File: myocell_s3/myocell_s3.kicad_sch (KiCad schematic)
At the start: 14 parts, among them J1 Conn_01x08, J5 Battery Connector JC2, J7 USB_C_Receptacle_USB2.0_16P

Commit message: scheme main table updated
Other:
- title: MYOCELL 8: EMG ADC board -> MYOCELL_S3: EMG ADC board
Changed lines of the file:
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@@
 	(paper "A4")
 	(title_block
-		(title "MYOCELL 8: EMG ADC board")
-		(date "2024-10-17")
+		(title "MYOCELL_S3: EMG ADC board")
+		(date "2025-12-24")
 		(rev "Rev 01")
 		(company "MIREA")
-		(comment 1 "2-8 ADC channels based on ADS1292(8)")
-		(comment 2 "CPU: ESP32 WROOM")
+		(comment 1 "4(8) ADC channels based on ADS1298")
+		(comment 2 "CPU: ESP32-S3 WROOM")
 	)
 	(text "esp32-s3 is spi master\nmiso - master in, slave out\nmosi - master out, slave in"

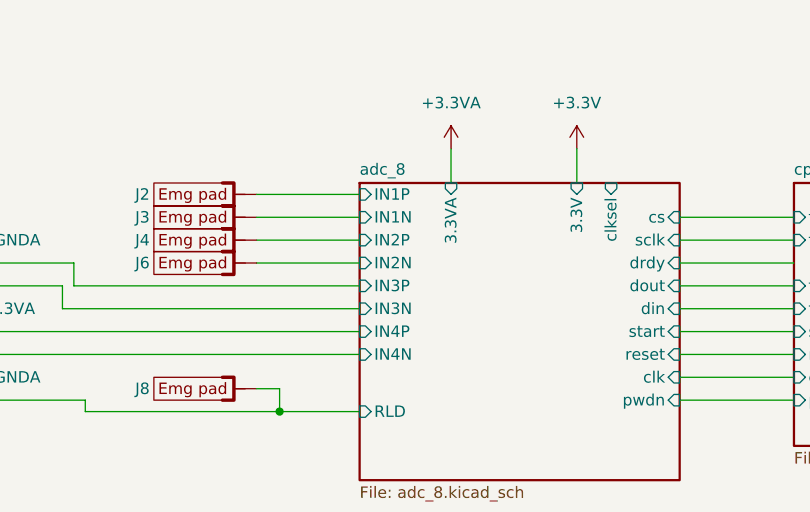
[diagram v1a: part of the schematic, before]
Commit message: emg filters updated
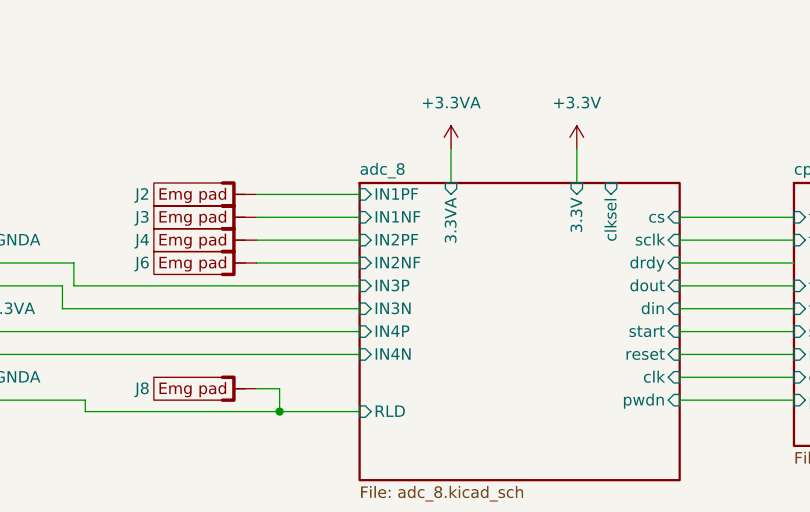
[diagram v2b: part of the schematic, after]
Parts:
- J2, J3, J4, J6, J8: value (none) -> ~
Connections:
- net adc_8/IN1N renamed adc_8/IN1NF
- net adc_8/IN1P renamed adc_8/IN1PF
- net adc_8/IN2N renamed adc_8/IN2NF
- net adc_8/IN2P renamed adc_8/IN2PF
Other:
- sheet adc_8 ports: added IN1NF, IN1PF, IN2NF, IN2PF; removed IN1N, IN1P, IN2N, IN2P

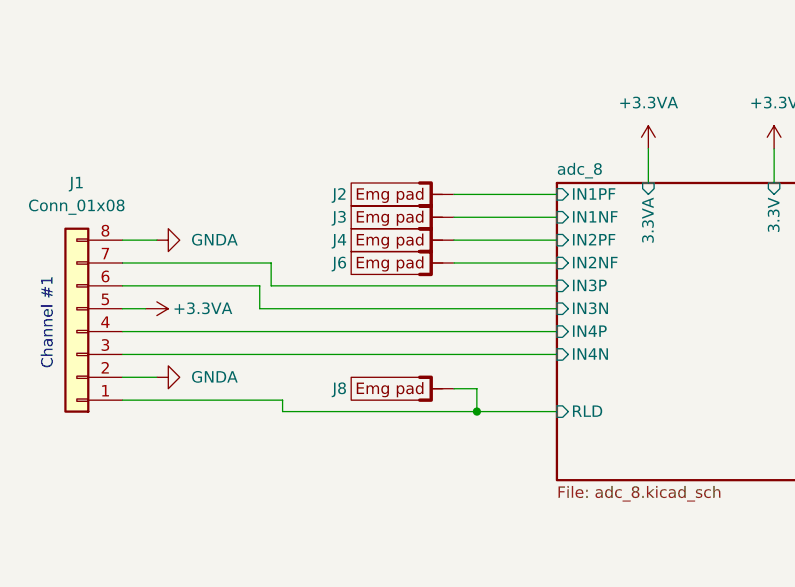
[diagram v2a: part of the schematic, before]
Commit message: schematic updated: channels 3,4 is onboard now
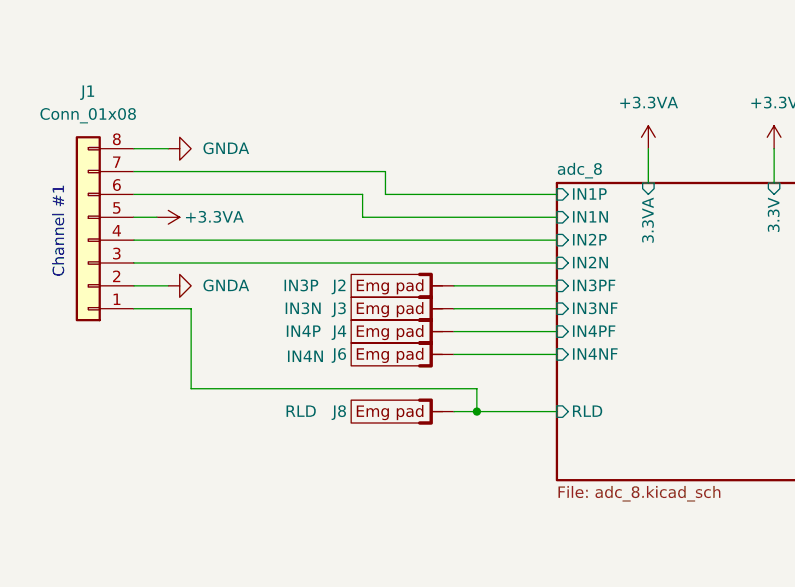
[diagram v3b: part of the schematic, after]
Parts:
- J2: value ~ -> IN3P
- J3: value ~ -> IN3N
- J4: value ~ -> IN4P
- J6: value ~ -> IN4N
- J8: value ~ -> RLD
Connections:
- net adc_8/IN1NF renamed adc_8/IN3NF
- net adc_8/IN1PF renamed adc_8/IN3PF
- net adc_8/IN2NF renamed adc_8/IN4NF
- net adc_8/IN2PF renamed adc_8/IN4PF
- net adc_8/IN3N renamed adc_8/IN1N
- net adc_8/IN3P renamed adc_8/IN1P
- net adc_8/IN4N renamed adc_8/IN2N
- net adc_8/IN4P renamed adc_8/IN2P
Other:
- sheet adc_8 ports: added IN1N, IN1P, IN2N, IN2P, IN3NF, IN3PF, IN4NF, IN4PF; removed IN1NF, IN1PF, IN2NF, IN2PF, IN3N, IN3P, IN4N, IN4P
- moved on the sheet: J1, J2, J3, J4, J6, J8

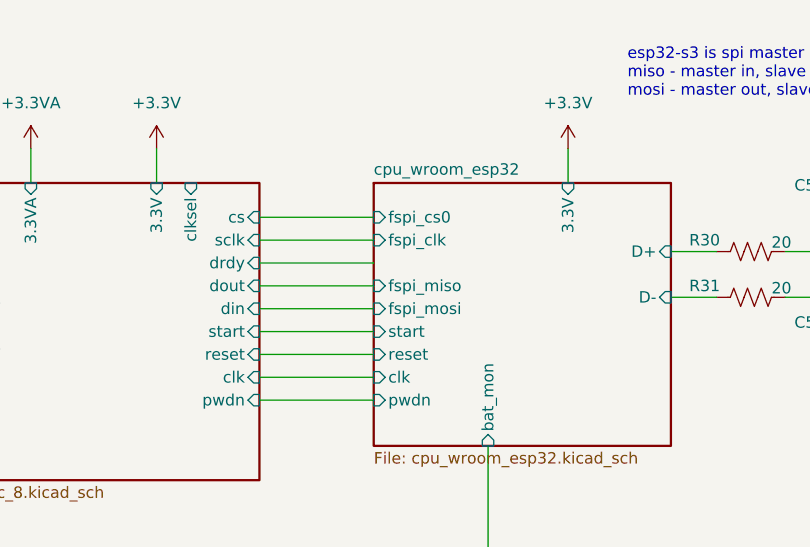
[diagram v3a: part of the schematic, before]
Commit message: drdy fixed
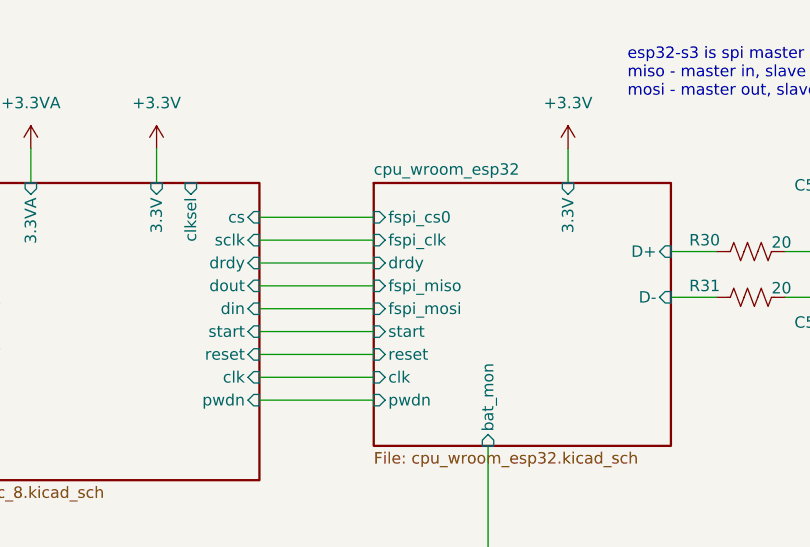
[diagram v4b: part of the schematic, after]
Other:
- sheet cpu_wroom_esp32 ports: added drdy; removed none
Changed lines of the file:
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@@
+	(wire
+		(pts
+			(xy 125.73 52.07) (xy 138.43 52.07)
+		)
+		(stroke
+			(width 0)
+			(type default)
+		)
+	)
 	(wire
 		(pts
@@
 		(pts
 			(xy 43.18 49.53) (xy 90.17 49.53)
-		)
-		(stroke
-			(width 0)
-			(type default)
-		)
-	)
-	(wire
-		(pts
-			(xy 125.73 52.07) (xy 138.43 52.07)
 		)
 		(stroke
@@
 			(effects
 				(font
+					(size 1.27 1.27)
+				)
+				(justify left)
+			)
+		)
+		(pin "drdy" input
+			(at 138.43 52.07 180)
+			(effects
+				(font

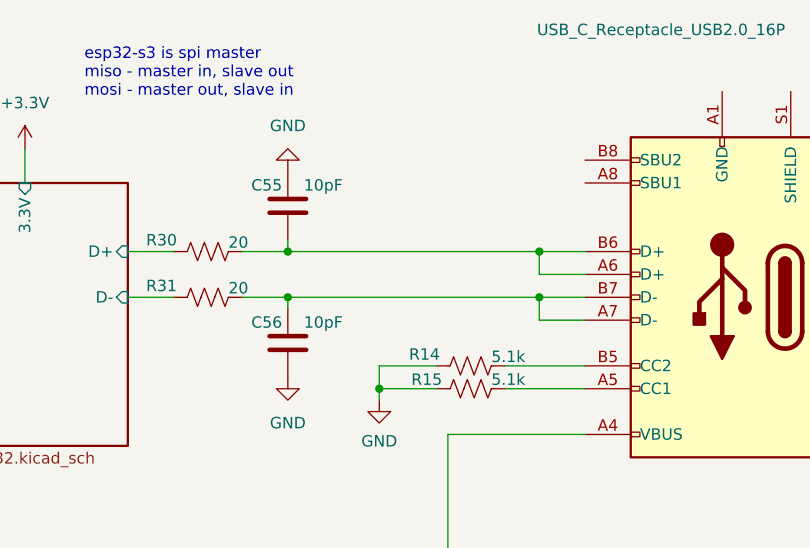
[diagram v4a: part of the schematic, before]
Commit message: spi routed length aligned to 20mm/pm0.5mm
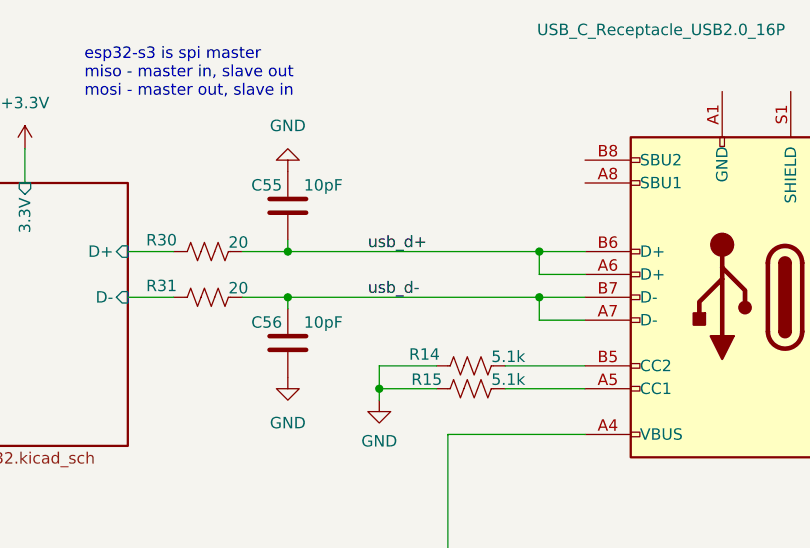
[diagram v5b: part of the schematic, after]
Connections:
- net usb_d+: now reaches C55.2, J7.A6 (D+), J7.B6 (D+), R30.2
- net usb_d-: now reaches C56.1, J7.A7 (D-), J7.B7 (D-), R31.2
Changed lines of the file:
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@@
+		)
+	)
+	(label "usb_d+"
+		(at 198.12 50.8 0)
+		(effects
+			(font
+				(size 1.27 1.27)
+			)
+			(justify left bottom)
+		)
+	)
+	(label "usb_d-"
+		(at 198.12 55.88 0)
+		(effects
+			(font
+				(size 1.27 1.27)
+			)
+			(justify left bottom)
 		)
 	)

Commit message: tracing ADS1298
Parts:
- added R34: 100k, Resistor_SMD:R_0805_2012Metric_Pad1.20x1.40mm_HandSolder, symbol Device:R_US
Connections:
- net GND: now also J7.A1 (GND), J7.A12 (GND), J7.B1 (GND), J7.B12 (GND), R34.1
- net at J7.S1 (SHIELD): now also R34.2
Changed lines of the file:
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@@
+	)
+	(junction
+		(at 237.49 30.48)
+		(diameter 0)
+		(color 0 0 0 0)
 	)
 	(junction
@@
 	(wire
 		(pts
+			(xy 231.14 30.48) (xy 237.49 30.48)
+		)
+		(stroke
+			(width 0)
+			(type default)
+		)
+	)
+	(wire
+		(pts
 			(xy 43.18 57.15) (xy 49.53 57.15)
 		)
@@
 	(wire
 		(pts
+			(xy 245.11 30.48) (xy 245.11 33.02)
+		)
+		(stroke
+			(width 0)
+			(type default)
+		)
+	)
+	(wire
+		(pts
 			(xy 222.25 53.34) (xy 217.17 53.34)
 		)
@@
 		(pts
 			(xy 43.18 39.37) (xy 46.99 39.37)
+		)
+		(stroke
+			(width 0)
+			(type default)
+		)
+	)
+	(wire
+		(pts
+			(xy 237.49 30.48) (xy 237.49 33.02)
 		)
 		(stroke
@@
 	(symbol
 		(lib_id "power:GND")
+		(at 231.14 30.48 270)
+		(unit 1)
+		(exclude_from_sim no)
+		(in_bom yes)
+		(on_board yes)
+		(dnp no)
+		(fields_autoplaced yes)
+		(property "Reference" "#PWR06"
+			(at 224.79 30.48 0)
+			(effects
+				(font
+					(size 1.27 1.27)
+				)
+				(hide yes)
+			)
+		)
+		(property "Value" "GND"
+			(at 227.33 30.4799 90)
+			(effects
+				(font
+					(size 1.27 1.27)
+				)
+				(justify right)
+			)
+		)
+		(property "Footprint" ""
+			(at 231.14 30.48 0)
+			(effects
+				(font
+					(size 1.27 1.27)
+				)
+				(hide yes)
+			)
+		)
+		(property "Datasheet" ""
+			(at 231.14 30.48 0)
+			(effects
+				(font
+					(size 1.27 1.27)
+				)
+				(hide yes)
+			)
+		)
+		(property "Description" "Power symbol creates a global label with name \"GND\" , ground"
+			(at 231.14 30.48 0)
+			(effects
+				(font
+					(size 1.27 1.27)
+				)
+				(hide yes)
+			)
+		)
+		(pin "1"
+		)
+		(instances
+			(project "myocell_s3"
+				(path "/871ff10b-bde5-471c-b91a-de58aa271388"
+					(reference "#PWR06")
+					(unit 1)
+				)
+			)
+		)
+	)
+	(symbol
+		(lib_id "power:GND")
 		(at 176.53 114.3 0)
 		(unit 1)
@@
 					(unit 1)
 				)
+			)
+		)
+	)
+	(symbol
+		(lib_id "Device:R_US")
+		(at 241.3 30.48 90)
+		(unit 1)
+		(exclude_from_sim no)
+		(in_bom yes)
+		(on_board yes)
+		(dnp no)
+		(property "Reference" "R34"
+			(at 234.442 29.21 90)
+			(effects
+				(font
+					(size 1.27 1.27)
+				)
+				(justify right)
+			)
+		)
+		(property "Value" "100k"
+			(at 243.586 29.464 90)
+			(effects
+				(font
+					(size 1.27 1.27)
+				)
+				(justify right)
+			)
+		)
+		(property "Footprint" "Resistor_SMD:R_0805_2012Metric_Pad1.20x1.40mm_HandSolder"
+			(at 241.554 29.464 90)
+			(effects
+				(font
+					(size 1.27 1.27)
+				)
+				(hide yes)
+			)
+		)
+		(property "Datasheet" "~"
+			(at 241.3 30.48 0)
+			(effects
+				(font
+					(size 1.27 1.27)
+				)
+				(hide yes)
+			)
+		)
+		(property "Description" "Resistor, US symbol"
+			(at 241.3 30.48 0)
+			(effects
+				(font
+					(size 1.27 1.27)
+				)
+				(hide yes)
+			)
+		)
+		(pin "1"
+		)
+		(pin "2"
+		)
+		(instances
+			(project "myocell_s3"
+				(path "/871ff10b-bde5-471c-b91a-de58aa271388"
+					(reference "R34")
+					(unit 1)
+				)

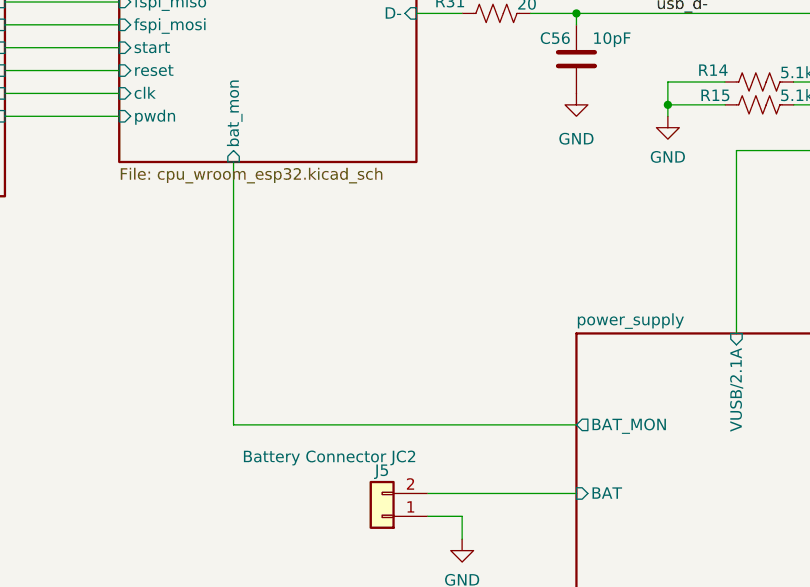
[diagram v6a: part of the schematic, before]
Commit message: placing polygons
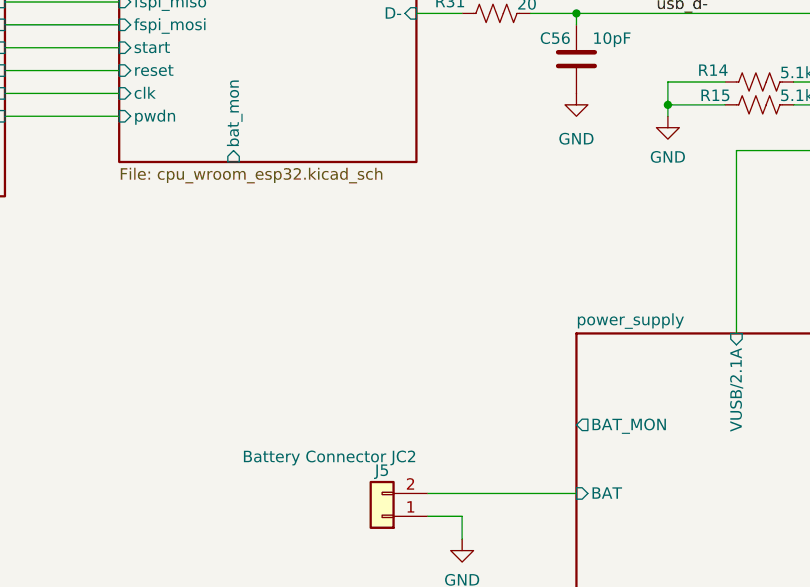
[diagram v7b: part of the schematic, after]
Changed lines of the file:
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@@
-	(wire
-		(pts
-			(xy 151.13 101.6) (xy 189.23 101.6)
-		)
-		(stroke
-			(width 0)
-			(type default)
-		)
-	)
 	(wire
 		(pts
@@
 		)
 		(stroke
-			(width 0)
-			(type default)
-		)
-	)
-	(wire
-		(pts
-			(xy 151.13 101.6) (xy 151.13 72.39)
-		)
-		(stroke

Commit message: DRC
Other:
- sheet power_supply ports: added bat_mon; removed BAT_MON
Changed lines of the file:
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@@
+	(wire
+		(pts
+			(xy 189.23 100.33) (xy 151.13 100.33)
+		)
+		(stroke
+			(width 0)
+			(type default)
+		)
+	)
 	(wire
 		(pts
@@
 		(pts
 			(xy 43.18 39.37) (xy 46.99 39.37)
+		)
+		(stroke
+			(width 0)
+			(type default)
+		)
+	)
+	(wire
+		(pts
+			(xy 151.13 100.33) (xy 151.13 72.39)
 		)
 		(stroke
@@
 			)
 		)
-		(pin "BAT_MON" output
-			(at 189.23 101.6 180)
-			(effects
-				(font
+		(pin "bat_mon" input
+			(at 189.23 100.33 180)
+			(effects
+				(font
